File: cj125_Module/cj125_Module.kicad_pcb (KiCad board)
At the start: 2 copper layers, 56 x 22 mm, 32 parts, among them J1 Conn_02x20_Odd_Even, Q1 buk 100-50, U1 TS5A3166DCKR, U2 TS5A3166DCKR, U3 CJ125

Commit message: DRAFT
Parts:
- moved Q1 45.0 mm to (26.7, 24.1), turned to 180 degrees
- moved R7 27.0 mm to (40.4, 34.4)
- moved C7 20.5 mm to (40.5, 35.7)
- moved R16 19.9 mm to (57.1, 32.4)
- moved C2 18.6 mm to (42.5, 33.7), turned to 45 degrees
- moved R6 18.0 mm to (38.7, 34.3), turned to 90 degrees
- moved C5 15.8 mm to (40.3, 25.1), turned to 135 degrees
- moved R10 15.2 mm to (34.9, 23.5), turned to 0 degrees
- moved R11 14.8 mm to (41.3, 26.7), turned to 225 degrees
- moved C3 14.3 mm to (52.1, 35.2), turned to 90 degrees
- moved R18 14.1 mm to (61.6, 33.0), turned to 270 degrees
- moved R17 13.2 mm to (43.5, 25.1), turned to 315 degrees
- moved R8 12.7 mm to (54.0, 34.3), turned to 225 degrees
- moved C4 11.9 mm to (52.7, 24.8), turned to 135 degrees
- moved R9 10.9 mm to (48.3, 21.6), turned to 0 degrees
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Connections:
- J1 pad 1: Net-(J1-Pad1) -> GND
- J1 pad 10: Net-(J1-Pad10) -> /LSU-HEAT-GATE
- J1 pad 11: Net-(J1-Pad11) -> /4.2_4.9
- J1 pad 12: Net-(J1-Pad12) -> /4.2_4.9
- J1 pad 13: Net-(J1-Pad13) -> /CJ125_UR-1
- J1 pad 14: Net-(J1-Pad14) -> /CJ125_UR-1
- J1 pad 15: Net-(J1-Pad15) -> /CJ125-1-SCK
- J1 pad 16: Net-(J1-Pad16) -> /CJ125-1-SCK
- J1 pad 17: Net-(J1-Pad17) -> /CJ125-1-SO
- J1 pad 18: Net-(J1-Pad18) -> /CJ125-1-SO
- J1 pad 19: Net-(J1-Pad19) -> /CJ125-1-SI
- J1 pad 2: Net-(J1-Pad2) -> GND
- J1 pad 20: Net-(J1-Pad20) -> /CJ125-1-SI
- J1 pad 21: Net-(J1-Pad21) -> /CJ125-1-SS
- J1 pad 22: Net-(J1-Pad22) -> /CJ125-1-SS
- J1 pad 23: Net-(J1-Pad23) -> /LSUVM1
- J1 pad 24: Net-(J1-Pad24) -> /LSUVM1
- J1 pad 25: Net-(J1-Pad25) -> /LSUIP1
- J1 pad 26: Net-(J1-Pad26) -> /LSUIP1
- J1 pad 27: Net-(J1-Pad27) -> /LSUUN1
- J1 pad 28: Net-(J1-Pad28) -> /LSUUN1
- J1 pad 29: Net-(J1-Pad29) -> /LSUIA1
- J1 pad 3: Net-(J1-Pad3) -> /5V
- J1 pad 30: Net-(J1-Pad30) -> /LSUIA1
- J1 pad 31: Net-(J1-Pad31) -> /CJ125-UA-1
- J1 pad 32: Net-(J1-Pad32) -> /CJ125-UA-1
- J1 pad 33: Net-(J1-Pad33) -> (no net)
- J1 pad 34: Net-(J1-Pad34) -> (no net)
- J1 pad 35: Net-(J1-Pad35) -> (no net)
- J1 pad 36: Net-(J1-Pad36) -> (no net)
- J1 pad 37: Net-(J1-Pad37) -> (no net)
- J1 pad 38: Net-(J1-Pad38) -> (no net)
- J1 pad 39: Net-(J1-Pad39) -> GND
- J1 pad 4: Net-(J1-Pad4) -> /5V
- J1 pad 40: Net-(J1-Pad40) -> GND
- J1 pad 5: Net-(J1-Pad5) -> /CJ125_HEATER-1
- J1 pad 6: Net-(J1-Pad6) -> /CJ125_HEATER-1
- J1 pad 7: Net-(J1-Pad7) -> /CJ125_HEATER-1
- J1 pad 8: Net-(J1-Pad8) -> /CJ125_HEATER-1
- J1 pad 9: Net-(J1-Pad9) -> /LSU-HEAT-GATE
- U1 pad 5: /5V -> (no net)
- U3 pad 13: (no net) -> /CJ125-1-SCK
- U3 pad 15: (no net) -> /CJ125-1-SI
- U3 pad 17: (no net) -> /CJ125-1-SS
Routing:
- net /5V: track 0.00 -> 52.5 mm, vias 0 -> 2
- net Net-(R4-Pad1): track 0.00 -> 44.8 mm
- net /LSUUN1: track 0.00 -> 36.1 mm
- net /CJ125_HEATER-1: track 0.00 -> 35.5 mm
- net /LSU-HEAT-GATE: track 0.00 -> 33.7 mm, vias 0 -> 1
- net /LSUVM1: track 0.00 -> 32.0 mm, vias 0 -> 1
- net /LSUIA1: track 0.00 -> 31.4 mm, vias 0 -> 2
- net /LSUIP1: track 0.00 -> 28.9 mm
- net /4.2_4.9: track 0.00 -> 12.2 mm
- net Net-(R6-Pad2): track 0.00 -> 12.2 mm
- net Net-(R10-Pad2): track 0.00 -> 10.8 mm
- net /CJ125-UA-1: track 0.00 -> 10.2 mm
- net /NO: track 0.00 -> 9.51 mm
- net /CJ125-1-SCK: track 0.00 -> 8.56 mm
- net /CJ125_UR-1: track 0.00 -> 7.21 mm
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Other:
- board text added: "4.#"
- board text added: "GATE"
- board text added: "HT1"
- board text added: "IA1"
- board text added: "IP1"
- board text added: "SCK"
- board text added: "SI"
- board text added: "SO"
- board text added: "SS"
- board text added: "UA1"
- board text added: "UN1"
- board text added: "UR"
- board text added: "VM1"
- board text added: "WIDEBAND CONTROLLER MODULE R0.1 RUSEFI"
- board text removed: "WIDEBAND CONTROLLER MODULE"

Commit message: R0.1
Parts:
- added D1: D_Schottky, Diode_SMD:D_SMF, F.Cu at (21.6, 30.5)
- added D2: LED, LED_SMD:LED_0603_1608Metric, F.Cu at (21.0, 34.9)
- added D3: D_Schottky, Diode_SMD:D_SMF, F.Cu at (25.4, 33.7)
- added D4: LED, LED_SMD:LED_0603_1608Metric, F.Cu at (22.2, 37.9)
- added R20: 4.7K, Resistor_SMD:R_0402_1005Metric, F.Cu at (22.2, 41.3)
- added R21: 1K, Resistor_SMD:R_0402_1005Metric, F.Cu at (22.2, 40.0)
- J1: footprint Connector_PinHeader_2.54mm:PinHeader_2x20_P2.54mm_Vertical -> Connector_PinHeader_2.54mm:PinHeader_2x16_P2.54mm_Vertical
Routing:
- net /CJ125_HEATER-1: track 35.5 -> 42.9 mm
- net Net-(D2-Pad1): track 0.00 -> 5.89 mm
- net /5V: track 52.5 -> 57.3 mm
- net Net-(D3-Pad1): track 0.00 -> 4.69 mm
- net GND: track 1.38 -> 5.30 mm, vias 22 -> 25
- net Net-(D1-Pad1): track 0.00 -> 2.47 mm
- net Net-(D4-Pad1): track 0.00 -> 1.47 mm
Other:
- board size 56 x 22 mm -> 45.4 x 22 mm
- board text added: "1"
- board text added: "4"

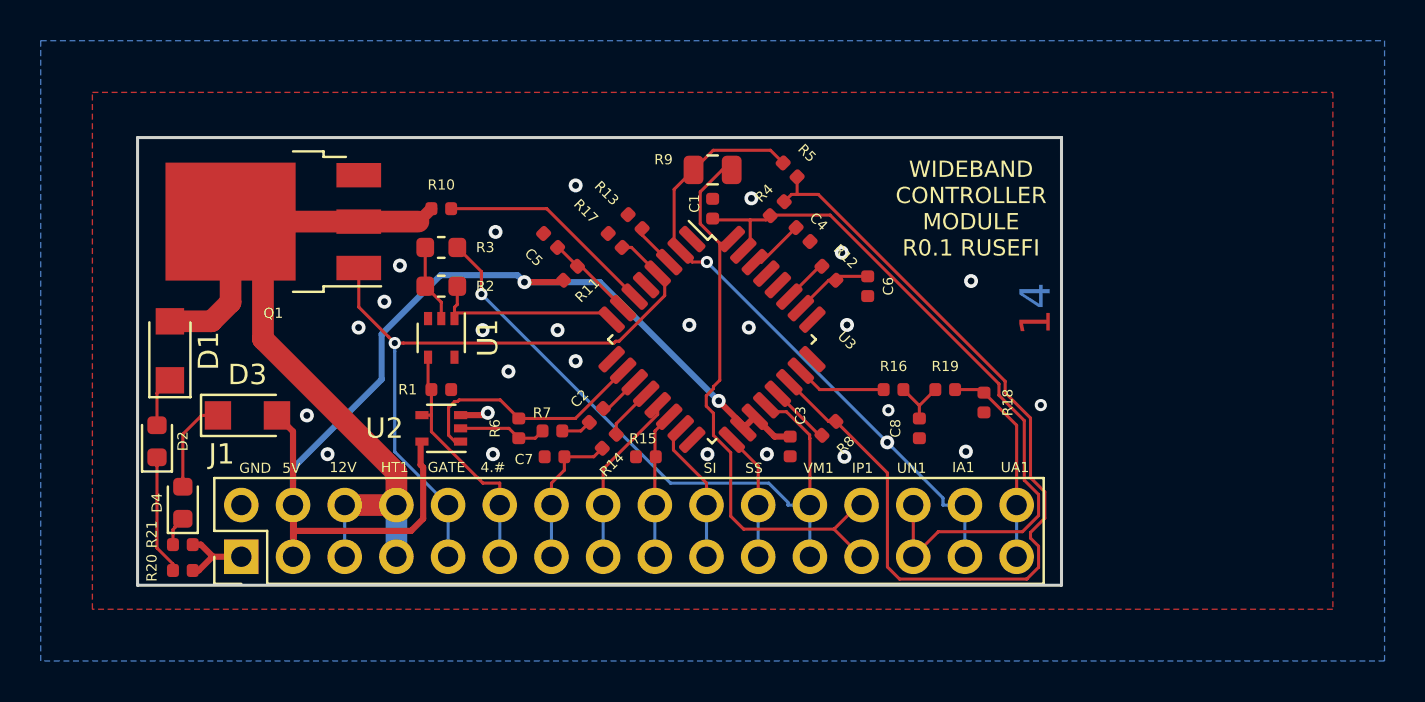
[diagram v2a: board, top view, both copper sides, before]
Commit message: Connected pin 5 to 5V
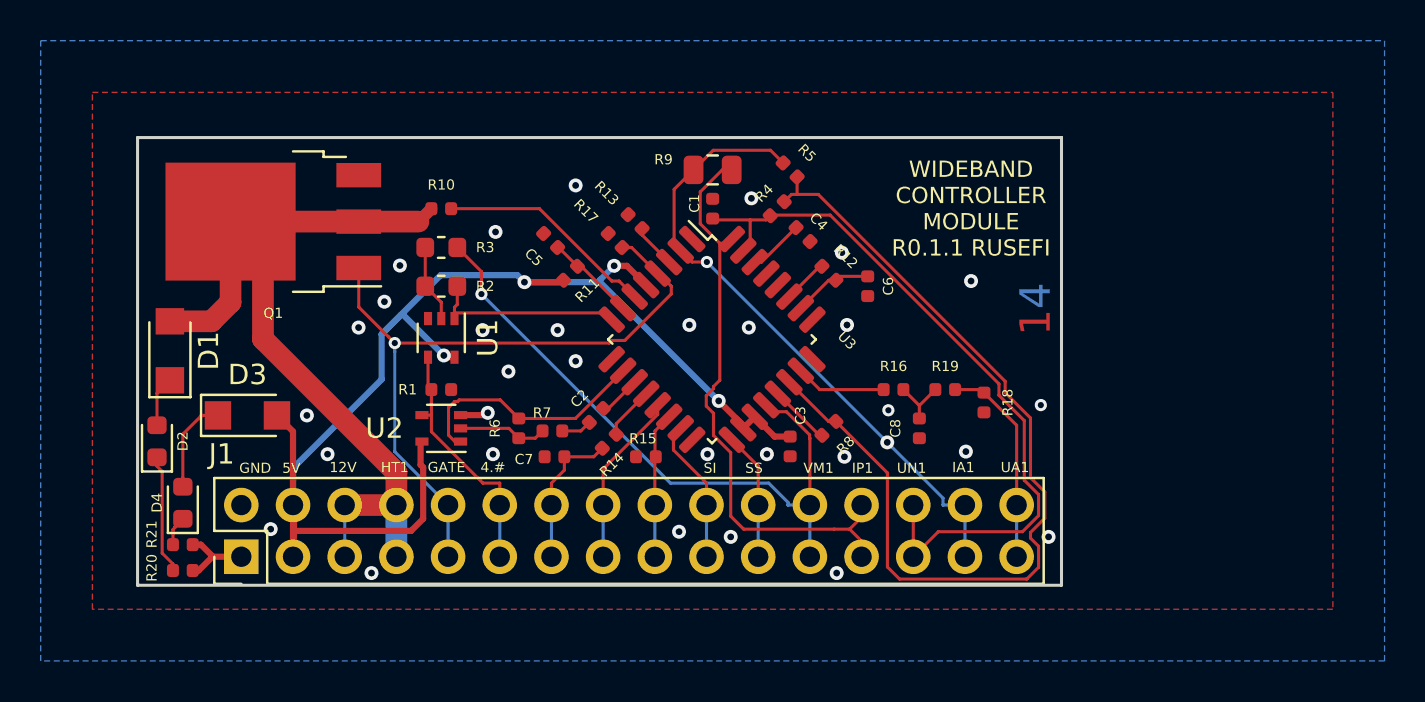
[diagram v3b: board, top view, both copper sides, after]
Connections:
- U1 pad 5: (no net) -> /5V
- U3 pad 5: (no net) -> /5V
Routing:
- net /5V: track 57.3 -> 65.2 mm, vias 2 -> 4
- net /LSU-HEAT-GATE: track 33.7 -> 34.7 mm
- net GND: vias 25 -> 31
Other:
- board text added: "WIDEBAND CONTROLLER MODULE R0.1.1 RUSEFI"
- board text removed: "WIDEBAND CONTROLLER MODULE R0.1 RUSEFI"
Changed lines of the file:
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@@
     (thickness 1.6)
     (drawings 39)
-    (tracks 290)
+    (tracks 312)
     (zones 0)
     (modules 38)
@@
   (title_block
     (title "Wideband Module")
-    (date 2019-01-31)
-    (rev R0.1)
+    (date 2020-05-03)
+    (rev R0.1.1)
     (company "Ruud Bilelektro for rusEFI")
   )
@@
       (effects (font (size 0.5 0.5) (thickness 0.075)))
     )
-    (pad 5 smd rect (at 0.95 -0.65 270) (size 0.65 0.4) (layers F.Cu F.Paste F.Mask))
+    (pad 5 smd rect (at 0.95 -0.65 270) (size 0.65 0.4) (layers F.Cu F.Paste F.Mask)
+      (net 13 /5V))
     (pad 4 smd rect (at 0.95 0.65 270) (size 0.65 0.4) (layers F.Cu F.Paste F.Mask)
       (net 12 /4.2_4.9))
@@
     (pad 6 smd roundrect (at -4.175 1.2 315) (size 1.5 0.5) (layers F.Cu F.Paste F.Mask) (roundrect_rratio 0.25)
       (net 25 "Net-(R10-Pad2)"))
-    (pad 5 smd roundrect (at -4.175 0.4 315) (size 1.5 0.5) (layers F.Cu F.Paste F.Mask) (roundrect_rratio 0.25))
+    (pad 5 smd roundrect (at -4.175 0.4 315) (size 1.5 0.5) (layers F.Cu F.Paste F.Mask) (roundrect_rratio 0.25)
+      (net 13 /5V))
     (pad 4 smd roundrect (at -4.175 -0.4 315) (size 1.5 0.5) (layers F.Cu F.Paste F.Mask) (roundrect_rratio 0.25)
       (net 6 /LSU-HEAT-GATE))
@@
     (effects (font (size 0.5 0.5) (thickness 0.1)) (justify mirror))
   )
-  (gr_text "WIDEBAND \nCONTROLLER \nMODULE\nR0.1 RUSEFI\n" (at 60.96 23.495) (layer F.SilkS)
+  (gr_text "WIDEBAND \nCONTROLLER \nMODULE\nR0.1.1 RUSEFI\n" (at 60.96 23.495) (layer F.SilkS)
     (effects (font (size 0.8 0.8) (thickness 0.15)))
   )
@@
   (via (at 60.96 27.051) (size 0.6858) (drill 0.3302) (layers F.Cu B.Cu) (net 1))
   (via (at 64.389 33.147) (size 0.6) (drill 0.3) (layers F.Cu B.Cu) (net 1))
+  (via (at 46.609 39.37) (size 0.6858) (drill 0.3302) (layers F.Cu B.Cu) (net 1))
+  (via (at 49.149 39.624) (size 0.6858) (drill 0.3302) (layers F.Cu B.Cu) (net 1))
+  (via (at 26.543 39.243) (size 0.6858) (drill 0.3302) (layers F.Cu B.Cu) (net 1))
+  (via (at 31.496 41.402) (size 0.6858) (drill 0.3302) (layers F.Cu B.Cu) (net 1))
+  (via (at 54.356 41.402) (size 0.6858) (drill 0.3302) (layers F.Cu B.Cu) (net 1))
+  (via (at 64.77 39.624) (size 0.6858) (drill 0.3302) (layers F.Cu B.Cu) (net 1))
   (segment (start 50.1066 24.0471) (end 48.3271 24.0471) (width 0.1524) (layer F.Cu) (net 2))
   (segment (start 48.3271 24.0471) (end 48.26 23.98) (width 0.1524) (layer F.Cu) (net 2))
@@
   (segment (start 21.59 29.03) (end 23.6368 29.03) (width 1.0668) (layer F.Cu) (net 5))
   (segment (start 35.26 40.6) (end 35.26 38.06) (width 0.1524) (layer B.Cu) (net 6))
-  (segment (start 43.663668 30.008332) (end 43.505012 30.008332) (width 0.1524) (layer F.Cu) (net 6))
   (segment (start 32.639 35.439) (end 32.639 30.523264) (width 0.1524) (layer B.Cu) (net 6))
   (segment (start 35.26 38.06) (end 32.639 35.439) (width 0.1524) (layer B.Cu) (net 6))
   (segment (start 32.339001 29.799001) (end 32.639 30.099) (width 0.1524) (layer F.Cu) (net 6))
-  (segment (start 43.505012 30.008332) (end 43.414344 30.099) (width 0.1524) (layer F.Cu) (net 6))
-  (segment (start 43.414344 30.099) (end 33.063264 30.099) (width 0.1524) (layer F.Cu) (net 6))
   (segment (start 30.87 26.41) (end 30.87 28.33) (width 0.1524) (layer F.Cu) (net 6))
   (segment (start 44.2757 25.4) (end 45.9052 27.0295) (width 0.1524) (layer F.Cu) (net 6))
   (segment (start 43.815 25.4) (end 44.2757 25.4) (width 0.1524) (layer F.Cu) (net 6))
   (segment (start 30.87 28.33) (end 32.339001 29.799001) (width 0.1524) (layer F.Cu) (net 6))
-  (segment (start 33.063264 30.099) (end 32.639 30.099) (width 0.1524) (layer F.Cu) (net 6))
   (segment (start 32.639 30.523264) (end 32.639 30.099) (width 0.1524) (layer B.Cu) (net 6))
-  (segment (start 45.9052 27.0295) (end 45.9052 27.7668) (width 0.1524) (layer F.Cu) (net 6))
   (via (at 32.639 30.099) (size 0.6) (drill 0.3) (layers F.Cu B.Cu) (net 6))
-  (segment (start 45.9052 27.7668) (end 43.663668 30.008332) (width 0.1524) (layer F.Cu) (net 6))
+  (segment (start 46.228 27.305) (end 45.607986 26.684986) (width 0.1524) (layer F.Cu) (net 6))
+  (segment (start 45.607986 26.684986) (end 45.560672 26.684986) (width 0.1524) (layer F.Cu) (net 6))
+  (segment (start 43.18 30.099) (end 43.307 29.972) (width 0.1524) (layer F.Cu) (net 6))
+  (segment (start 32.639 30.099) (end 43.18 30.099) (width 0.1524) (layer F.Cu) (net 6))
+  (segment (start 43.942 29.972) (end 46.228 27.686) (width 0.1524) (layer F.Cu) (net 6))
+  (segment (start 43.307 29.972) (end 43.942 29.972) (width 0.1524) (layer F.Cu) (net 6))
+  (segment (start 46.228 27.686) (end 46.228 27.305) (width 0.1524) (layer F.Cu) (net 6))
   (segment (start 53.04 38.06) (end 51.9611 38.06) (width 0.1524) (layer B.Cu) (net 7))
   (segment (start 51.9611 38.06) (end 51.9611 37.925) (width 0.1524) (layer B.Cu) (net 7))
@@
   (segment (start 47.6512 22.6712) (end 47.6512 24.2374) (width 0.1524) (layer F.Cu) (net 9))
   (segment (start 47.6512 24.2374) (end 48.6123 25.1985) (width 0.1524) (layer F.Cu) (net 9))
-  (segment (start 54.229 39.249) (end 55.58 40.6) (width 0.1524) (layer F.Cu) (net 9))
-  (segment (start 54.229 39.243) (end 54.229 39.249) (width 0.1524) (layer F.Cu) (net 9))
-  (segment (start 55.412 38.06) (end 55.58 38.06) (width 0.1524) (layer F.Cu) (net 9))
-  (segment (start 54.229 39.243) (end 55.412 38.06) (width 0.1524) (layer F.Cu) (net 9))
   (segment (start 49.149 38.608) (end 49.784 39.243) (width 0.1524) (layer F.Cu) (net 9))
   (segment (start 49.784 39.243) (end 54.229 39.243) (width 0.1524) (layer F.Cu) (net 9))
@@
   (segment (start 48.3015 33.5473) (end 48.3015 34.6327) (width 0.1524) (layer F.Cu) (net 9))
   (segment (start 47.9486 32.6892) (end 47.9486 33.1944) (width 0.1524) (layer F.Cu) (net 9))
+  (segment (start 55.58 39.832) (end 55.58 40.6) (width 0.1524) (layer F.Cu) (net 9))
+  (segment (start 54.229 39.243) (end 54.991 39.243) (width 0.1524) (layer F.Cu) (net 9))
+  (segment (start 54.991 39.243) (end 55.58 39.832) (width 0.1524) (layer F.Cu) (net 9))
+  (segment (start 55.58 38.654) (end 55.58 38.06) (width 0.1524) (layer F.Cu) (net 9))
+  (segment (start 54.991 39.243) (end 55.58 38.654) (width 0.1524) (layer F.Cu) (net 9))
   (segment (start 46.1264 33.7207) (end 45.4279 34.4192) (width 0.1524) (layer F.Cu) (net 10))
   (segment (start 45.4279 34.4192) (end 45.4279 35.8521) (width 0.1524) (layer F.Cu) (net 10))
@@
   (segment (start 31.996095 31.884905) (end 27.64 36.241) (width 0.3048) (layer B.Cu) (net 13))
   (segment (start 31.996095 29.663407) (end 31.996095 31.884905) (width 0.3048) (layer B.Cu) (net 13))
+  (via (at 43.420553 26.302447) (size 0.6858) (drill 0.3302) (layers F.Cu B.Cu) (net 13))
+  (segment (start 42.7228 27.1062) (end 42.7228 27.0002) (width 0.3048) (layer B.Cu) (net 13))
+  (segment (start 42.7228 27.0002) (end 43.420553 26.302447) (width 0.3048) (layer B.Cu) (net 13))
+  (segment (start 44.046761 26.302447) (end 44.994986 27.250672) (width 0.3048) (layer F.Cu) (net 13))
+  (segment (start 43.420553 26.302447) (end 44.046761 26.302447) (width 0.3048) (layer F.Cu) (net 13))
+  (via (at 35.052 30.7086) (size 0.6858) (drill 0.3302) (layers F.Cu B.Cu) (net 13))
+  (segment (start 35.575 30.795) (end 35.1384 30.795) (width 0.3048) (layer F.Cu) (net 13))
+  (segment (start 35.1384 30.795) (end 35.052 30.7086) (width 0.3048) (layer F.Cu) (net 13))
+  (segment (start 32.957502 28.702) (end 31.996095 29.663407) (width 0.3048) (layer B.Cu) (net 13))
+  (segment (start 35.052 30.7086) (end 33.0454 28.702) (width 0.3048) (layer B.Cu) (net 13))
+  (segment (start 33.0454 28.702) (end 32.957502 28.702) (width 0.3048) (layer B.Cu) (net 13))
   (segment (start 35.575 28.618) (end 42.9682 28.618) (width 0.1524) (layer F.Cu) (net 14))
   (segment (start 42.9682 28.618) (end 43.2979 28.9477) (width 0.1524) (layer F.Cu) (net 14))
@@
   (segment (start 51.465 32.5893) (end 53.5086 34.6329) (width 0.1524) (layer F.Cu) (net 24))
   (segment (start 53.5086 34.6329) (end 53.6321 34.6329) (width 0.1524) (layer F.Cu) (net 24))
-  (segment (start 44.4293 27.8164) (end 40.1079 23.495) (width 0.1524) (layer F.Cu) (net 25))
-  (segment (start 40.1079 23.495) (end 35.41 23.495) (width 0.1524) (layer F.Cu) (net 25))
+  (segment (start 39.751 23.495) (end 35.41 23.495) (width 0.1524) (layer F.Cu) (net 25))
+  (segment (start 44.4293 27.8164) (end 43.6639 27.051) (width 0.1524) (layer F.Cu) (net 25))
+  (segment (start 43.307 27.051) (end 39.751 23.495) (width 0.1524) (layer F.Cu) (net 25))
+  (segment (start 43.6639 27.051) (end 43.307 27.051) (width 0.1524) (layer F.Cu) (net 25))
   (segment (start 52.0307 27.8164) (end 53.52 26.3271) (width 0.1524) (layer F.Cu) (net 26))
   (segment (start 53.52 26.3271) (end 53.6321 26.3271) (width 0.1524) (layer F.Cu) (net 26))
@@
   (segment (start 20.955 32.565) (end 21.59 31.93) (width 0.1524) (layer F.Cu) (net 33))
   (segment (start 20.955 34.1375) (end 20.955 32.565) (width 0.1524) (layer F.Cu) (net 33))
-  (segment (start 20.955 40.17) (end 20.955 36.15) (width 0.1524) (layer F.Cu) (net 34))
+  (segment (start 21.209 36.404) (end 20.955 36.15) (width 0.1524) (layer F.Cu) (net 34))
+  (segment (start 21.74 41.275) (end 21.74 40.955) (width 0.1524) (layer F.Cu) (net 34))
   (segment (start 20.955 36.15) (end 20.955 35.7125) (width 0.1524) (layer F.Cu) (net 34))
-  (segment (start 21.74 40.955) (end 20.955 40.17) (width 0.1524) (layer F.Cu) (net 34))
-  (segment (start 21.74 41.275) (end 21.74 40.955) (width 0.1524) (layer F.Cu) (net 34))
+  (segment (start 21.209 40.424) (end 21.209 36.404) (width 0.1524) (layer F.Cu) (net 34))
+  (segment (start 21.74 40.955) (end 21.209 40.424) (width 0.1524) (layer F.Cu) (net 34))
   (segment (start 22.225 36.7225) (end 22.225 37.16) (width 0.1524) (layer F.Cu) (net 35))
   (segment (start 22.225 34.5776) (end 22.225 36.7225) (width 0.1524) (layer F.Cu) (net 35))
